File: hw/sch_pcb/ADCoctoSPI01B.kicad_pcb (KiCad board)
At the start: 2 copper layers, 70.6 x 70.6 mm, 80 parts, among them J1 SATA7-67491-1030, J10 SAS_mini_1888174, J11 +5V, J2 SATA7-67491-1030, J3 SATA7-67491-1030, J4 SATA7-67491-1030, J5 HEADER_1x02, J6 HEADER_1x02, J7 SATA7-67491-1030, J8 HEADER_2x04, J9 HEADER_1x02, M1 HOLE, M2 HOLE, M3 HOLE, M4 HOLE, U1 AFE5801, U2 LM1117MP-1,8/NO, U3 LM1117MP-3,3/NO

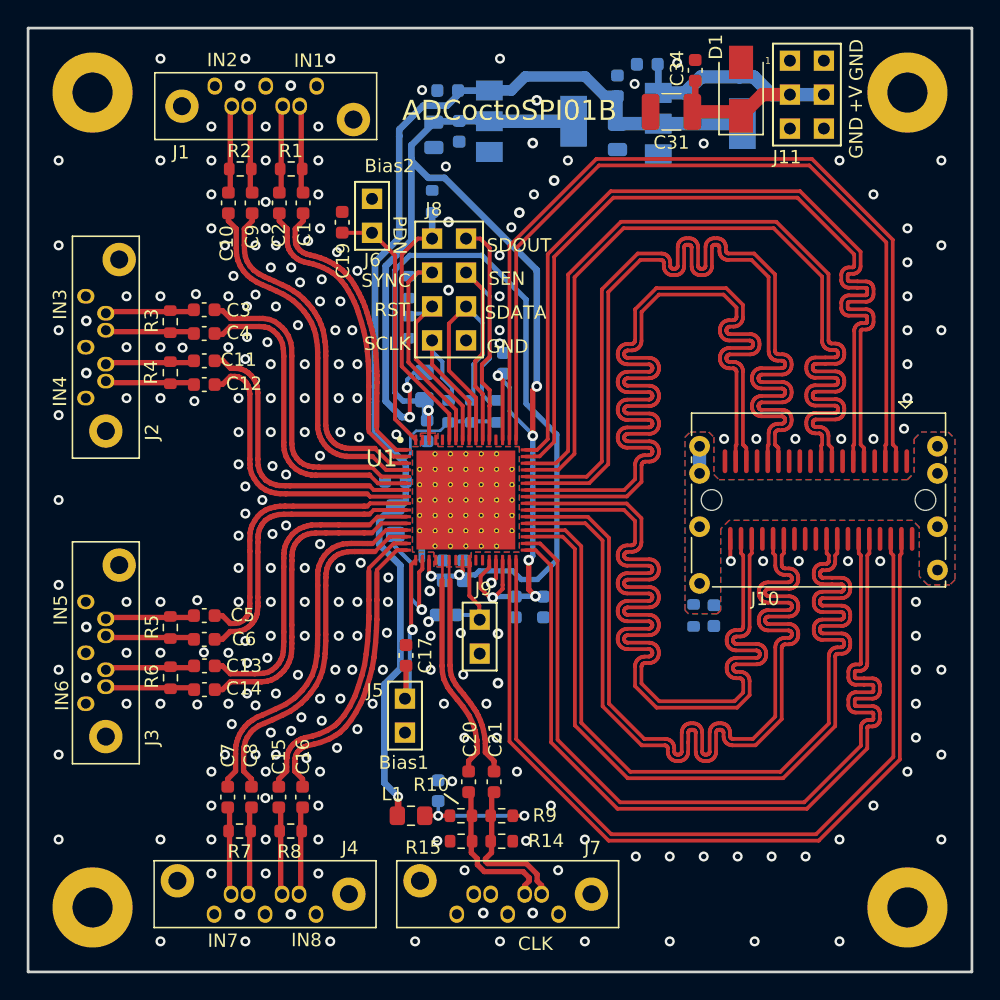
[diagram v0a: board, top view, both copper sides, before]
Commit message: doroutovani cest
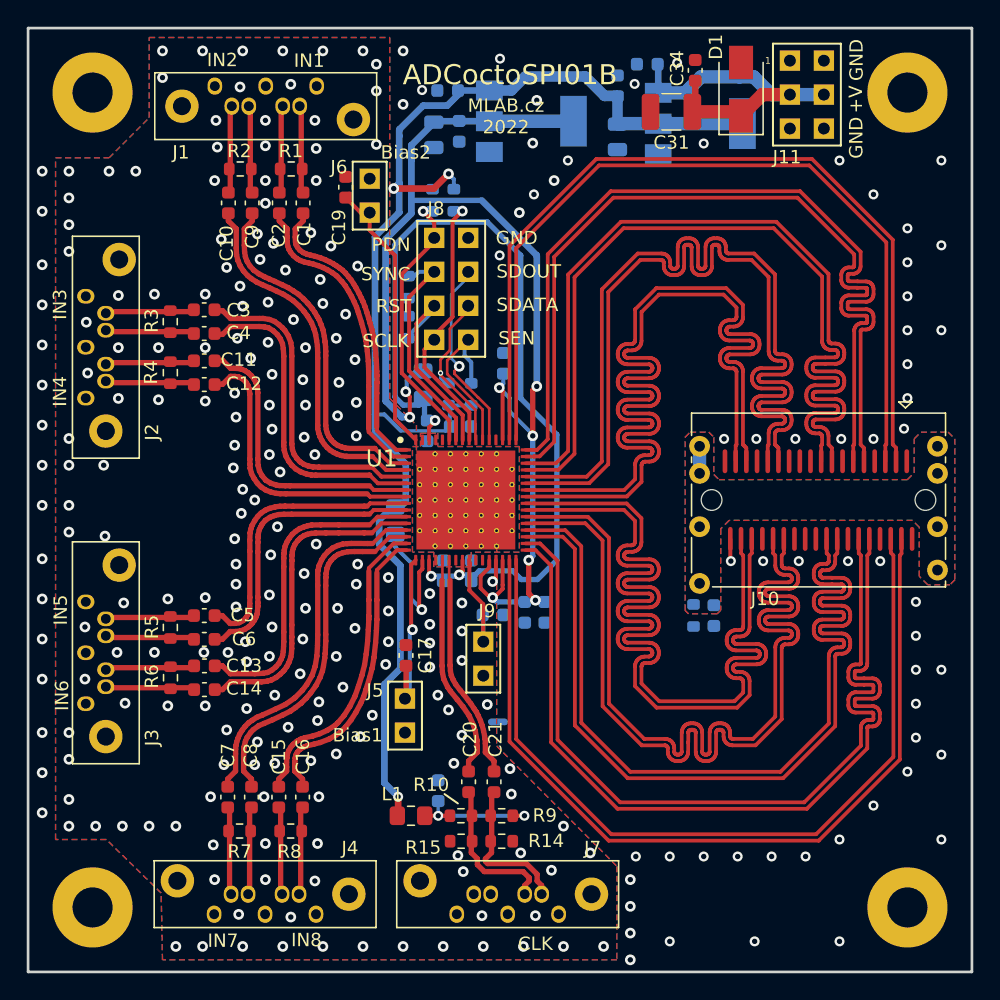
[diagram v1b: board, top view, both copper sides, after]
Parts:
- moved R16 15.8 mm to (91.8, 79.2), turned to -90 degrees
- moved JP1 13.8 mm to (95.1, 118.2), turned to 180 degrees
- moved C28 6.35 mm to (92.3, 96.1), turned to 0 degrees
- moved C22 3.50 mm to (94.7, 110.2), turned to 180 degrees
- moved C19 2.64 mm to (83.7, 78.2)
- moved R18 2.28 mm to (93.1, 93.7)
- moved R17 2.14 mm to (91.4, 93.7)
- moved J9 1.67 mm to (94.0, 113.5)
- moved J6 1.52 mm to (85.5, 78.8)
- moved C33 0.81 mm to (97.1, 110.0)
- moved C32 0.60 mm to (93.1, 106.9)
- moved C27 0.41 mm to (98.6, 110.0)
- moved J8 0.17 mm to (91.6, 85.8)
- moved L2 0.14 mm to (89.5, 93.0)
- moved R11 0.09 mm to (90.2, 79.2)
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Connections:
- C17 pad 1: GND -> GNDA
- C18 pad 2: GND -> GNDA
- C19 pad 2: GND -> GNDA
- J1 pad 1: GND -> GNDA
- J1 pad 4: GND -> GNDA
- J1 pad 7: GND -> GNDA
- J2 pad 1: GND -> GNDA
- J2 pad 4: GND -> GNDA
- J2 pad 7: GND -> GNDA
- J3 pad 1: GND -> GNDA
- J3 pad 4: GND -> GNDA
- J3 pad 7: GND -> GNDA
- J4 pad 1: GND -> GNDA
- J4 pad 4: GND -> GNDA
- J4 pad 7: GND -> GNDA
- J5 pad 2: GND -> GNDA
- J6 pad 2: GND -> GNDA
- J7 pad 1: GND -> GNDA
- J7 pad 4: GND -> GNDA
- J7 pad 7: GND -> GNDA
- J8 pad 2: Net-(J8-Pad2) -> GND
- J8 pad 8: GND -> Net-(R18-Pad2)
- J9 pad 2: GND -> unconnected-(J9-Pad2)
- R14 pad 1: GND -> GNDA
- R15 pad 1: GND -> GNDA
- R18 pad 2: Net-(J8-Pad4) -> Net-(R18-Pad2)
- U1 pad 53: Net-(J8-Pad2) -> Net-(J8-Pad4)
- U1 pad 54: Net-(J8-Pad4) -> Net-(R18-Pad2)
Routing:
- net Net-(J8-Pad2): track 16.9 -> 0.00 mm
- net Net-(R18-Pad2): track 0.00 -> 12.8 mm
- net Net-(J8-Pad4): track 24.9 -> 14.6 mm, vias 0 -> 1
- net DVDD3V3: track 95.1 -> 102.5 mm, vias 1 -> 3
- net Net-(J8-Pad7): track 13.8 -> 20.6 mm, vias 0 -> 1
- net Net-(R17-Pad2): track 19.3 -> 12.9 mm, vias 0 -> 1
- net AVDD: track 60.7 -> 65.4 mm
- net Net-(C19-Pad1): track 19.1 -> 21.1 mm
- net Net-(C22-Pad2): track 6.20 -> 8.13 mm
- net Net-(J8-Pad5): track 14.1 -> 16.0 mm
- net Net-(J8-Pad1): track 20.2 -> 20.8 mm, vias 0 -> 1
- net GND: track 3.65 -> 3.51 mm, vias 247 -> 77
- net GNDA: vias 0 -> 192
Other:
- board text added: "MLAB.cz 2022"

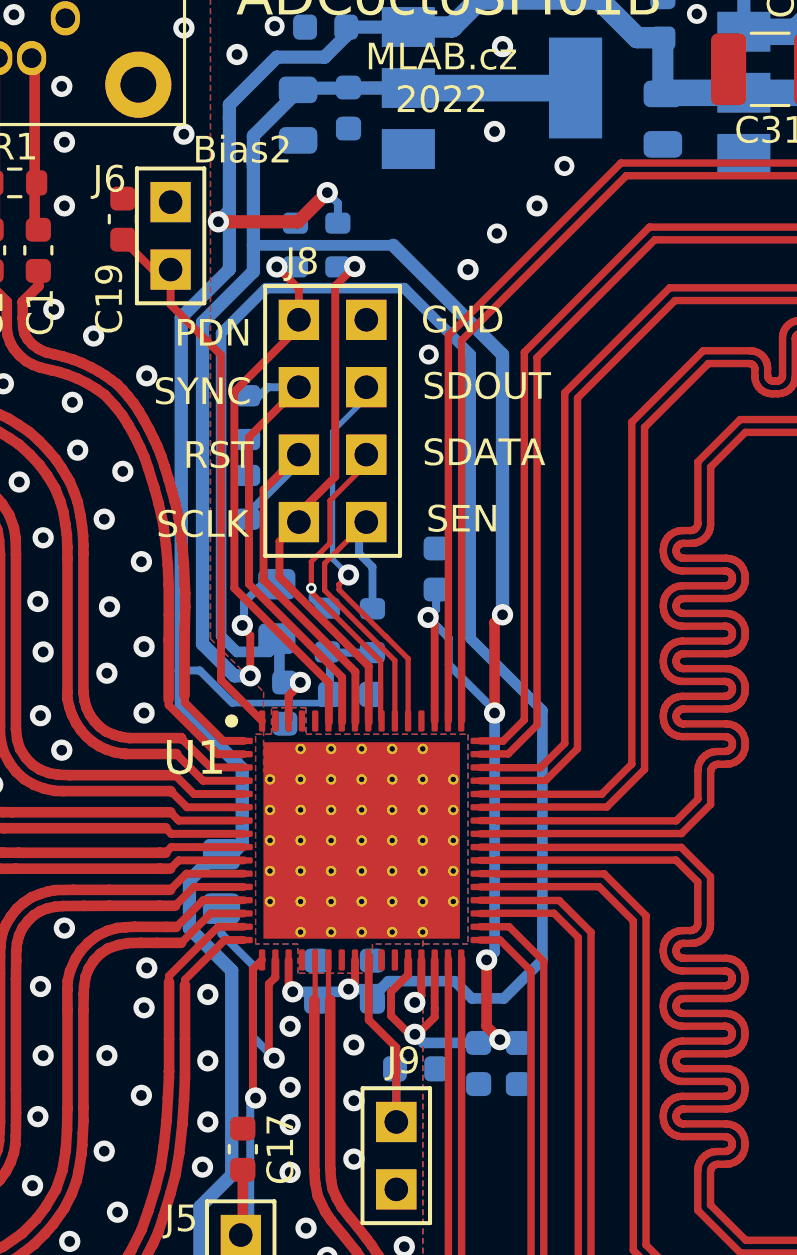
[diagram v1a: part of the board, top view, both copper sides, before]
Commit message: Improve GND layout.
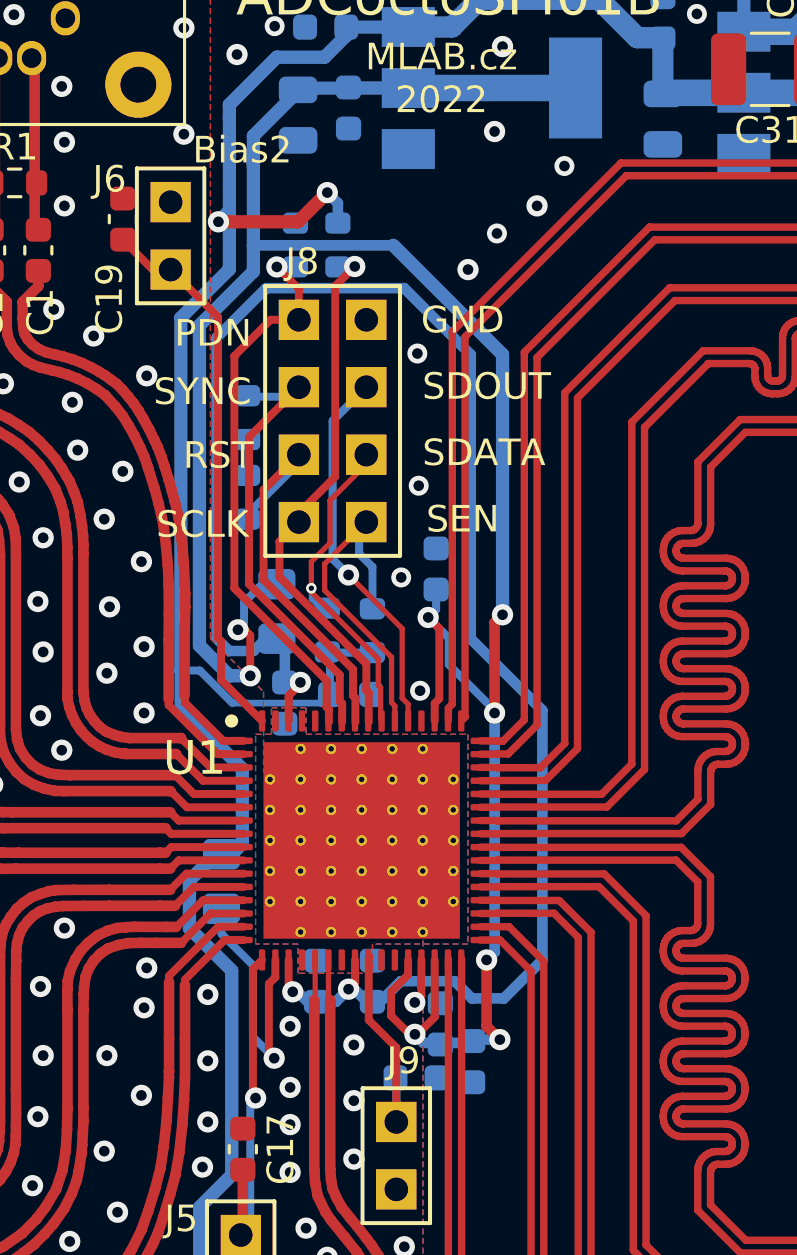
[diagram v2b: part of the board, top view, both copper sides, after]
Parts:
- moved C33 2.08 mm to (95.7, 108.5), turned to 90 degrees
- moved C27 1.73 mm to (96.9, 109.9)
- moved C22 0.34 mm to (94.7, 110.5)
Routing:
- net AVDD: track 65.4 -> 66.4 mm
- net Net-(J8-Pad1): track 20.8 -> 21.4 mm
- net GND: vias 77 -> 80

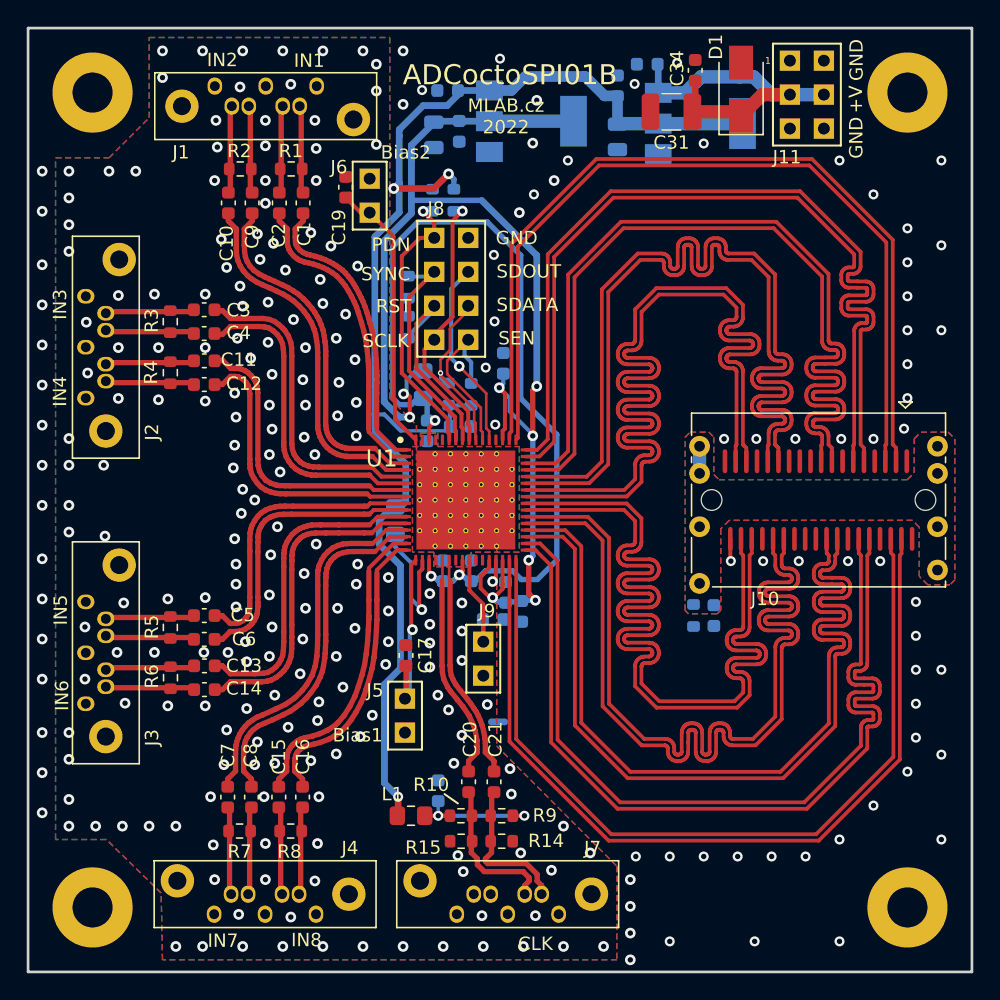
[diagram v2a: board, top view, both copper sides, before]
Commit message: uprava routovani, premisteni soucastek, AVDD k hodinam
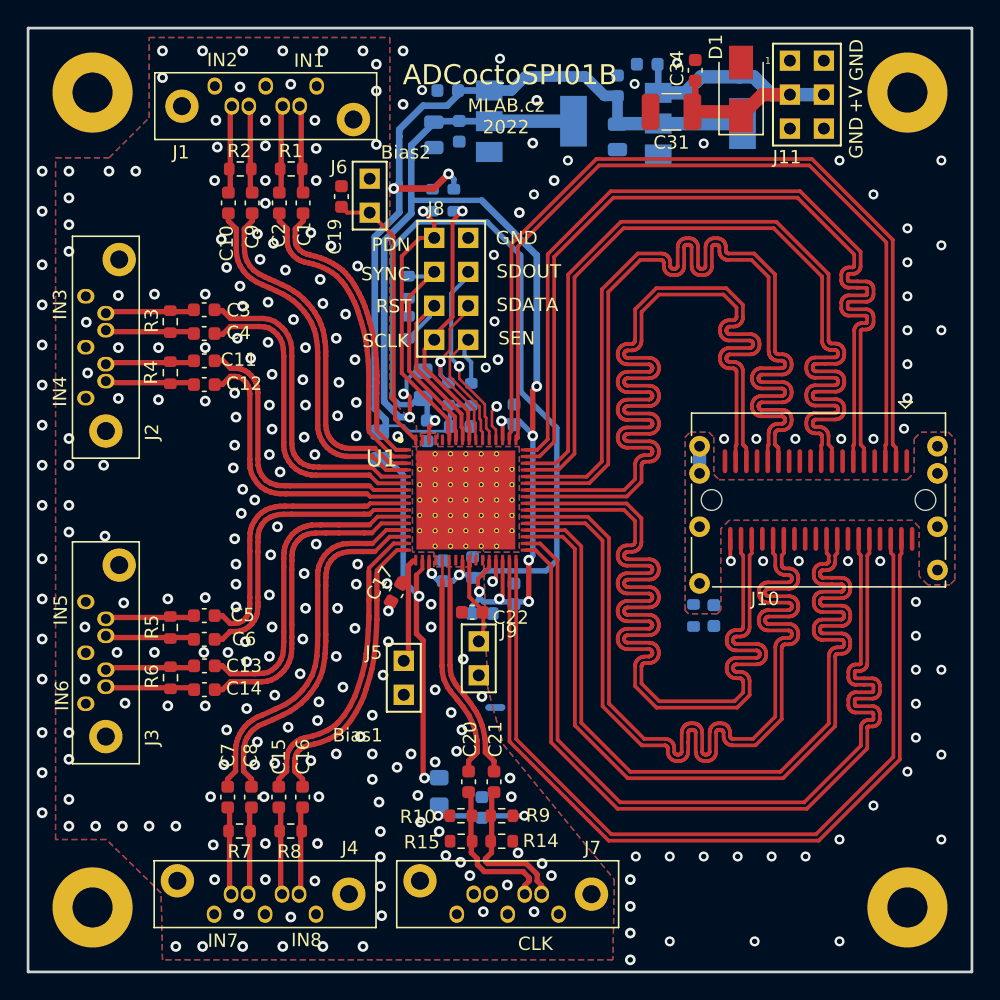
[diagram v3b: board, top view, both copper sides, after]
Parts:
- C22: moved to F.Cu
- L1: moved to B.Cu
- moved L3 5.71 mm to (86.2, 97.5)
- moved C17 4.76 mm to (87.5, 108.5), turned to 60 degrees
- moved C30 3.93 mm to (96.3, 95.2)
- moved C18 3.50 mm to (93.9, 124.6)
- moved J5 2.83 mm to (88.0, 114.9)
- moved L1 2.79 mm to (90.7, 123.4), turned to -90 degrees
- moved C33 2.35 mm to (93.9, 110.1), turned to 0 degrees
- moved C22 1.66 mm to (93.2, 110.0), turned to 0 degrees
- moved C27 1.43 mm to (96.3, 108.6), turned to 90 degrees
- moved JP1 1.10 mm to (94.9, 117.1)
- moved C19 0.76 mm to (83.4, 78.9)
- moved J9 0.34 mm to (93.7, 113.4)
- moved C32 0.27 mm to (93.2, 106.7)
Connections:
- C22 pad 1: GND -> GNDA
- J9 pad 2: unconnected-(J9-Pad2) -> GNDA
- L1 pad 1: DVDD3V3 -> AVDD3V3
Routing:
- net DVDD3V3: track 102.5 -> 69.9 mm, vias 3 -> 2
- net AVDD3V3: track 10.3 -> 29.9 mm, vias 1 -> 2
- net Net-(C17-Pad2): track 13.3 -> 8.28 mm, vias 1 -> 0
- net DVDD: track 97.3 -> 93.3 mm, vias 8 -> 9
- net GND: track 3.51 -> 6.28 mm, vias 80 -> 81
- net Net-(C22-Pad2): track 8.13 -> 6.42 mm
- net Net-(C18-Pad1): track 10.5 -> 9.18 mm
- net AVDD: track 66.4 -> 65.2 mm
- net Net-(J8-Pad6): track 12.9 -> 13.8 mm
- net Net-(J8-Pad7): track 20.6 -> 20.0 mm
- net GNDA: vias 192 -> 197

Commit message: drobne upravy routovani
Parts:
- moved L3 0.60 mm to (86.3, 97.0)
- moved J9 0.44 mm to (94.1, 113.4)
- moved C26 0.15 mm to (89.7, 96.5)
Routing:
- net AVDD: track 65.2 -> 64.5 mm
- net Net-(J8-Pad1): track 21.3 -> 20.7 mm
- net AVDD3V3: track 29.9 -> 30.5 mm
- net DVDD: track 93.3 -> 93.9 mm
- net Net-(J8-Pad5): track 16.0 -> 16.6 mm
- net Net-(J8-Pad6): track 13.8 -> 13.2 mm
- net GND: vias 81 -> 96
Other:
- board text added: "Vref"
